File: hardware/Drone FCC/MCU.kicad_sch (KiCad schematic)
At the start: 38 parts, among them SW101 SW RESET, U101 STM32F746ZGTx, Y101 12MHz, Y102 32.768kHz

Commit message: included all components on PCB
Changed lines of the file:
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@@
     (pin "2")
   )
-  (symbol (lib_id "Device:C_Small") (at 173.99 24.765 0) (unit 1)
+  (symbol (lib_id "Device:C_Small") (at 173.99 24.765 0) (mirror y) (unit 1)
     (in_bom yes) (on_board yes) (fields_autoplaced)
     (property "Reference" "C102" (id 0) (at 176.53 23.5012 0)
-      (effects (font (size 1.27 1.27)) (justify left))
+      (effects (font (size 1.27 1.27)) (justify right))
     )
     (property "Value" "100nF" (id 1) (at 176.53 26.0412 0)
-      (effects (font (size 1.27 1.27)) (justify left))
+      (effects (font (size 1.27 1.27)) (justify right))
     )
     (property "Footprint" "Capacitor_SMD:C_0402_1005Metric_Pad0.74x0.62mm_HandSolder" (id 2) (at 173.99 24.765 0)

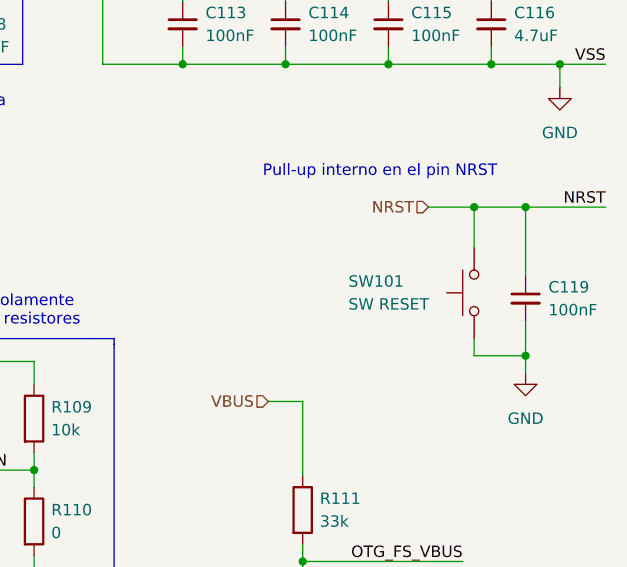
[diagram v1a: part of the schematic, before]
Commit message: add 3D models to footprints
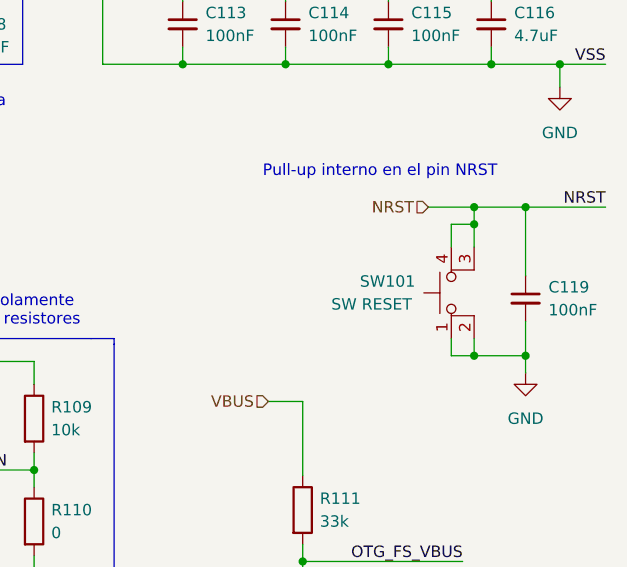
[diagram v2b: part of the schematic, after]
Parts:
- removed SW101: SW RESET, Button_Switch_SMD:SW_SPST_TL3305A, symbol Switch:SW_Push
- added SW101: SW RESET, TL3305AF160QG:SW_TL3305AF160QG, symbol Switch:SW_MEC_5E
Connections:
- net GND: now also SW101.1, SW101.2
- net NRST: now also SW101.3 (K), SW101.4 (A)

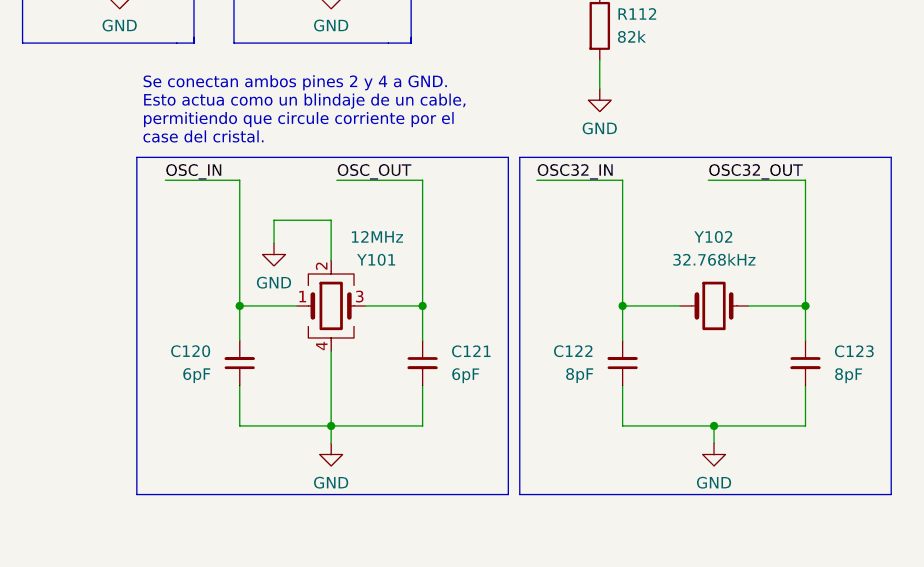
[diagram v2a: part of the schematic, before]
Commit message: routing of HSE crystal oscillator
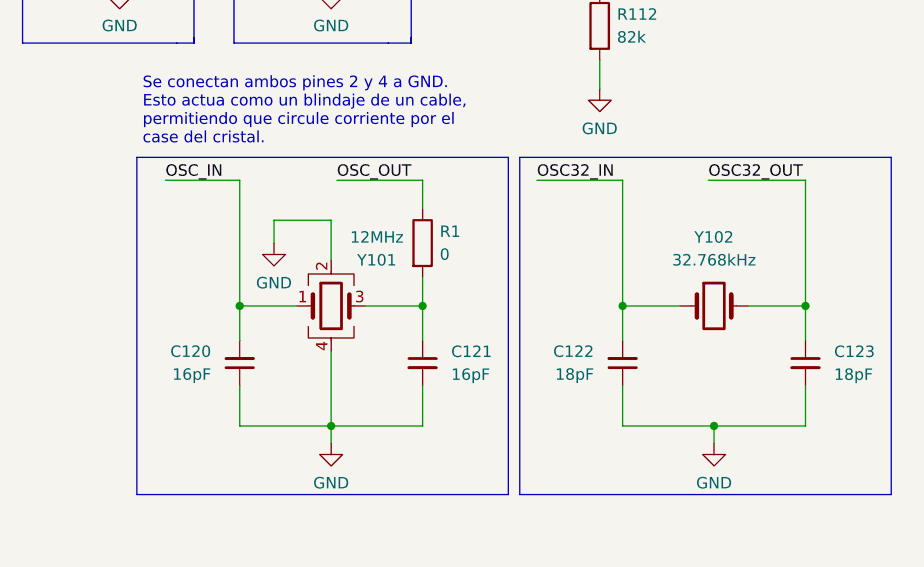
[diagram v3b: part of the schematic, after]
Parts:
- added R1: 0, Resistor_SMD:R_0402_1005Metric_Pad0.72x0.64mm_HandSolder, symbol Device:R
- C120, C121: value 6pF -> 16pF
- C122, C123: value 8pF -> 18pF
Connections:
- net OSC_OUT: now also R1.1; no longer C121.1, Y101.3
- new net: C121.1, R1.2, Y101.3
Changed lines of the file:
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@@
     (stroke (width 0) (type default) (color 0 0 0 0))
   )
-  (wire (pts (xy 229.87 127.635) (xy 229.87 141.605))
+  (wire (pts (xy 229.87 127.635) (xy 229.87 130.81))
     (stroke (width 0) (type default) (color 0 0 0 0))
   )
@@
   )
   (wire (pts (xy 25.4 83.82) (xy 43.18 83.82))
+    (stroke (width 0) (type default) (color 0 0 0 0))
+  )
+  (wire (pts (xy 229.87 138.43) (xy 229.87 141.605))
     (stroke (width 0) (type default) (color 0 0 0 0))
   )
@@
       (effects (font (size 1.27 1.27)) (justify right))
     )
-    (property "Value" "6pF" (id 1) (at 206.375 149.2185 0)
+    (property "Value" "16pF" (id 1) (at 206.375 149.2185 0)
       (effects (font (size 1.27 1.27)) (justify right))
     )
@@
       (effects (font (size 1.27 1.27)) (justify right))
     )
-    (property "Value" "8pF" (id 1) (at 248.92 149.2185 0)
+    (property "Value" "18pF" (id 1) (at 248.92 149.2185 0)
       (effects (font (size 1.27 1.27)) (justify right))
     )
@@
     )
     (property "Datasheet" "~" (id 3) (at 259.08 22.225 0)
+      (effects (font (size 1.27 1.27)) hide)
+    )
+    (pin "1")
+    (pin "2")
+  )
+  (symbol (lib_id "Device:R") (at 229.87 134.62 0) (unit 1)
+    (in_bom yes) (on_board yes) (fields_autoplaced)
+    (property "Reference" "R1" (id 0) (at 231.775 133.3499 0)
+      (effects (font (size 1.27 1.27)) (justify left))
+    )
+    (property "Value" "0" (id 1) (at 231.775 135.8899 0)
+      (effects (font (size 1.27 1.27)) (justify left))
+    )
+    (property "Footprint" "Resistor_SMD:R_0402_1005Metric_Pad0.72x0.64mm_HandSolder" (id 2) (at 228.092 134.62 90)
+      (effects (font (size 1.27 1.27)) hide)
+    )
+    (property "Datasheet" "~" (id 3) (at 229.87 134.62 0)
       (effects (font (size 1.27 1.27)) hide)
     )
@@
       (effects (font (size 1.27 1.27)) (justify left))
     )
-    (property "Value" "6pF" (id 1) (at 233.045 149.2312 0)
+    (property "Value" "16pF" (id 1) (at 233.045 149.2312 0)
       (effects (font (size 1.27 1.27)) (justify left))
     )
@@
       (effects (font (size 1.27 1.27)) (justify left))
     )
-    (property "Value" "8pF" (id 1) (at 275.59 149.2312 0)
-      (effects (font (size 1.27 1.27)) (justify left))
-    )
+    (property "Value" "18pF" (id 1) (at 275.59 149.2312 0)
+      (effects (font (size 1.27 1.27)) (justify left))
+    )

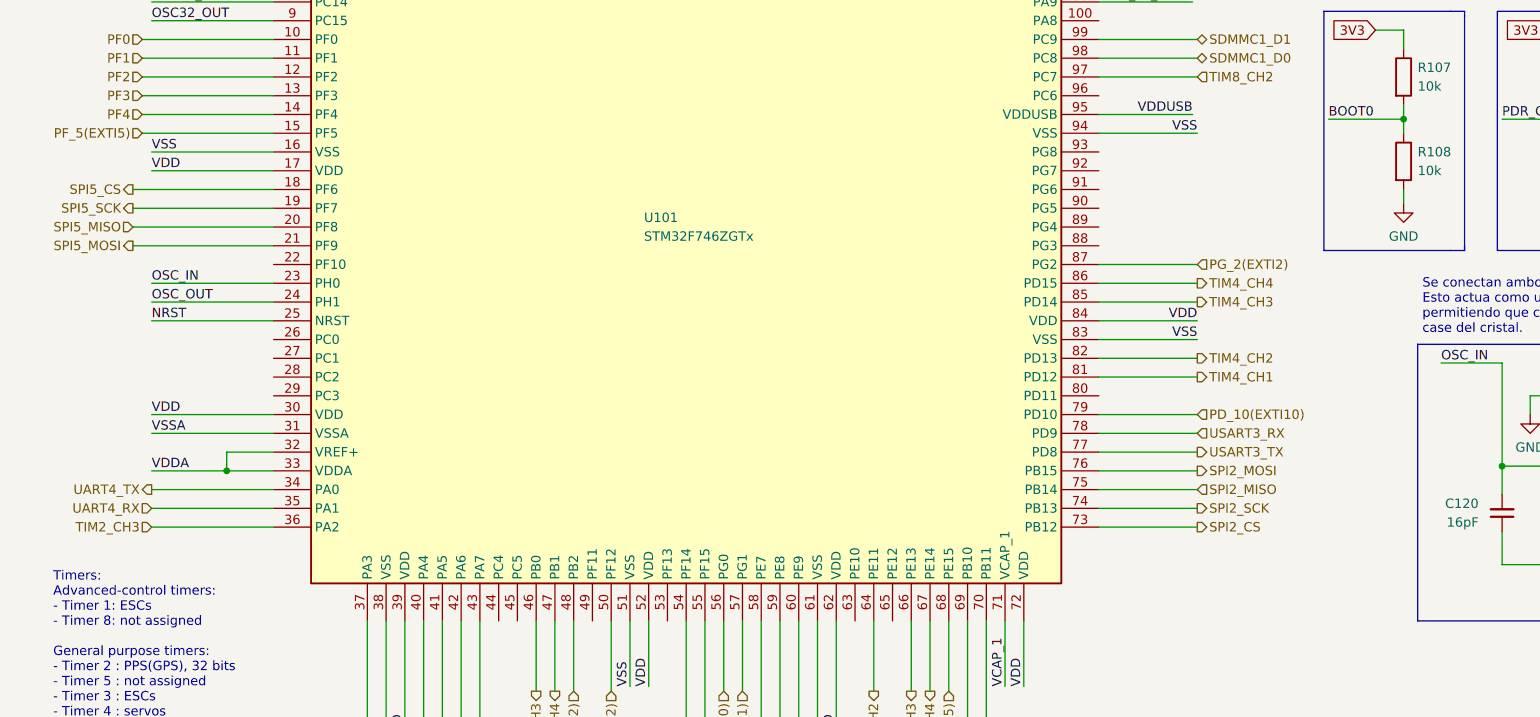
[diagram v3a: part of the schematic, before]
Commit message: add series resistor SPI buses
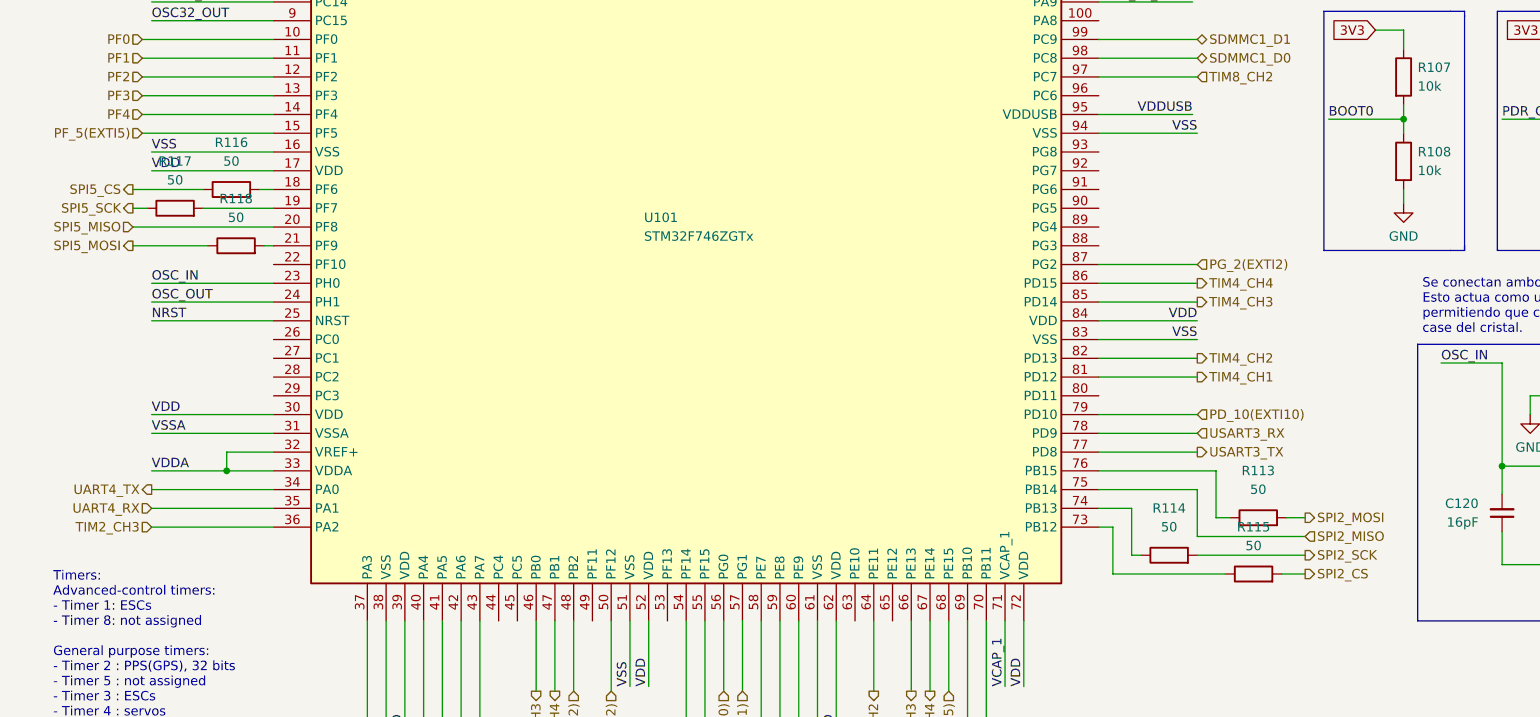
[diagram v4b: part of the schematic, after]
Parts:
- added R113, R114, R115, R116, R117, R118: 50, Resistor_SMD:R_0402_1005Metric_Pad0.72x0.64mm_HandSolder, symbol Device:R
- C119: footprint Capacitor_SMD:C_0603_1608Metric_Pad1.08x0.95mm_HandSolder -> Capacitor_SMD:C_0402_1005Metric_Pad0.74x0.62mm_HandSolder
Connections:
- net SPI2_CS: now also R115.2; no longer U101.73 (PB12)
- net SPI2_MOSI: now also R113.2; no longer U101.76 (PB15)
- net SPI2_SCK: now also R114.2; no longer U101.74 (PB13)
- net SPI5_CS: now also R116.1; no longer U101.18 (PF6)
- net SPI5_MOSI: now also R118.1; no longer U101.21 (PF9)
- net SPI5_SCK: now also R117.1; no longer U101.19 (PF7)
- new net: R117.2, U101.19 (PF7)
- new net: R114.1, U101.74 (PB13)
- new net: R116.2, U101.18 (PF6)
- new net: R118.2, U101.21 (PF9)
- new net: R115.1, U101.73 (PB12)
- new net: R113.1, U101.76 (PB15)

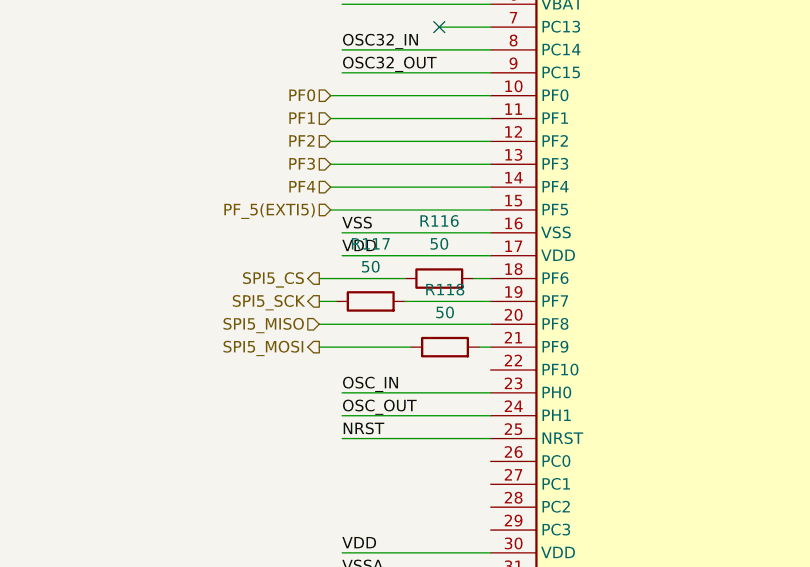
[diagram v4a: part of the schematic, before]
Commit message: add TVS diodes for SPI and ESD capacitors
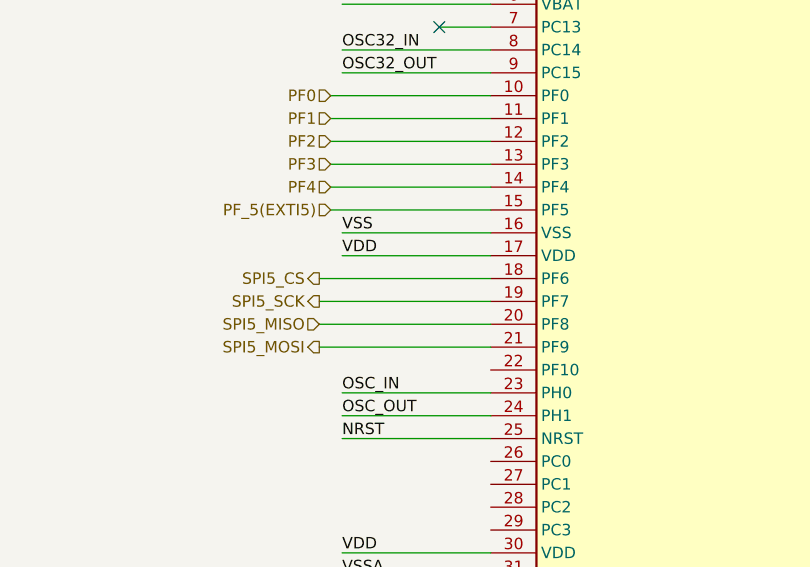
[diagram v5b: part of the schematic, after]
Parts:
- removed R116, R117, R118: 50, Resistor_SMD:R_0402_1005Metric_Pad0.72x0.64mm_HandSolder, symbol Device:R
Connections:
- net SPI5_CS: now also U101.18 (PF6)
- net SPI5_MOSI: now also U101.21 (PF9)
- net SPI5_SCK: now also U101.19 (PF7)
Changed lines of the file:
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@@
-    (stroke (width 0) (type default) (color 0 0 0 0))
-  )
-  (wire (pts (xy 24.13 111.76) (xy 34.29 111.76))
     (stroke (width 0) (type default) (color 0 0 0 0))
   )
@@
     (stroke (width 0) (type default) (color 0 0 0 0))
   )
-  (wire (pts (xy 33.655 106.68) (xy 43.18 106.68))
-    (stroke (width 0) (type default) (color 0 0 0 0))
-  )
   (wire (pts (xy 259.08 49.53) (xy 270.51 49.53))
     (stroke (width 0) (type default) (color 0 0 0 0))
@@
     (stroke (width 0) (type default) (color 0 0 0 0))
   )
-  (wire (pts (xy 41.91 111.76) (xy 43.18 111.76))
+  (wire (pts (xy 24.13 111.76) (xy 43.18 111.76))
     (stroke (width 0) (type default) (color 0 0 0 0))
   )
@@
     (stroke (width 0) (type default) (color 0 0 0 0))
   )
-  (wire (pts (xy 24.13 106.68) (xy 26.035 106.68))
+  (wire (pts (xy 24.13 106.68) (xy 43.18 106.68))
     (stroke (width 0) (type default) (color 0 0 0 0))
   )
@@
     (stroke (width 0) (type default) (color 0 0 0 0))
   )
-  (wire (pts (xy 41.275 104.14) (xy 43.18 104.14))
-    (stroke (width 0) (type default) (color 0 0 0 0))
-  )
   (polyline (pts (xy 208.915 80.01) (xy 226.06 80.01))
     (stroke (width 0) (type default) (color 0 0 0 0))
@@
     (stroke (width 0) (type default) (color 0 0 0 0))
   )
-  (wire (pts (xy 24.13 104.14) (xy 33.655 104.14))
+  (wire (pts (xy 24.13 104.14) (xy 43.18 104.14))
     (stroke (width 0) (type default) (color 0 0 0 0))
   )
@@
     )
     (property "Datasheet" "~" (id 3) (at 229.87 134.62 0)
-      (effects (font (size 1.27 1.27)) hide)
-    )
-    (pin "1")
-    (pin "2")
-  )
-  (symbol (lib_id "Device:R") (at 29.845 106.68 90) (unit 1)
-    (in_bom yes) (on_board yes) (fields_autoplaced)
-    (property "Reference" "R117" (id 0) (at 29.845 100.33 90))
-    (property "Value" "50" (id 1) (at 29.845 102.87 90))
-    (property "Footprint" "Resistor_SMD:R_0402_1005Metric_Pad0.72x0.64mm_HandSolder" (id 2) (at 29.845 108.458 90)
-      (effects (font (size 1.27 1.27)) hide)
-    )
-    (property "Datasheet" "~" (id 3) (at 29.845 106.68 0)
       (effects (font (size 1.27 1.27)) hide)
     )
@@
     (pin "99")
   )
-  (symbol (lib_id "Device:R") (at 37.465 104.14 90) (unit 1)
-    (in_bom yes) (on_board yes) (fields_autoplaced)
-    (property "Reference" "R116" (id 0) (at 37.465 97.79 90))
-    (property "Value" "50" (id 1) (at 37.465 100.33 90))
-    (property "Footprint" "Resistor_SMD:R_0402_1005Metric_Pad0.72x0.64mm_HandSolder" (id 2) (at 37.465 105.918 90)
-      (effects (font (size 1.27 1.27)) hide)
-    )
-    (property "Datasheet" "~" (id 3) (at 37.465 104.14 0)
-      (effects (font (size 1.27 1.27)) hide)
-    )
-    (pin "1")
-    (pin "2")
-  )
   (symbol (lib_id "Device:C_Small") (at 236.22 22.225 0) (unit 1)
     (in_bom yes) (on_board yes) (fields_autoplaced)
@@
       (effects (font (size 1.27 1.27)) hide)
     )
-    (pin "1")
-    (pin "2")
-  )
-  (symbol (lib_id "Device:R") (at 38.1 111.76 90) (unit 1)
-    (in_bom yes) (on_board yes) (fields_autoplaced)
-    (property "Reference" "R118" (id 0) (at 38.1 105.41 90))
-    (property "Value" "50" (id 1) (at 38.1 107.95 90))
-    (property "Footprint" "Resistor_SMD:R_0402_1005Metric_Pad0.72x0.64mm_HandSolder" (id 2) (at 38.1 113.538 90)
-      (effects (font (size 1.27 1.27)) hide)
-    )
-    (property "Datasheet" "~" (id 3) (at 38.1 111.76 0)
-      (effects (font (size 1.27 1.27)) hide)
-    )

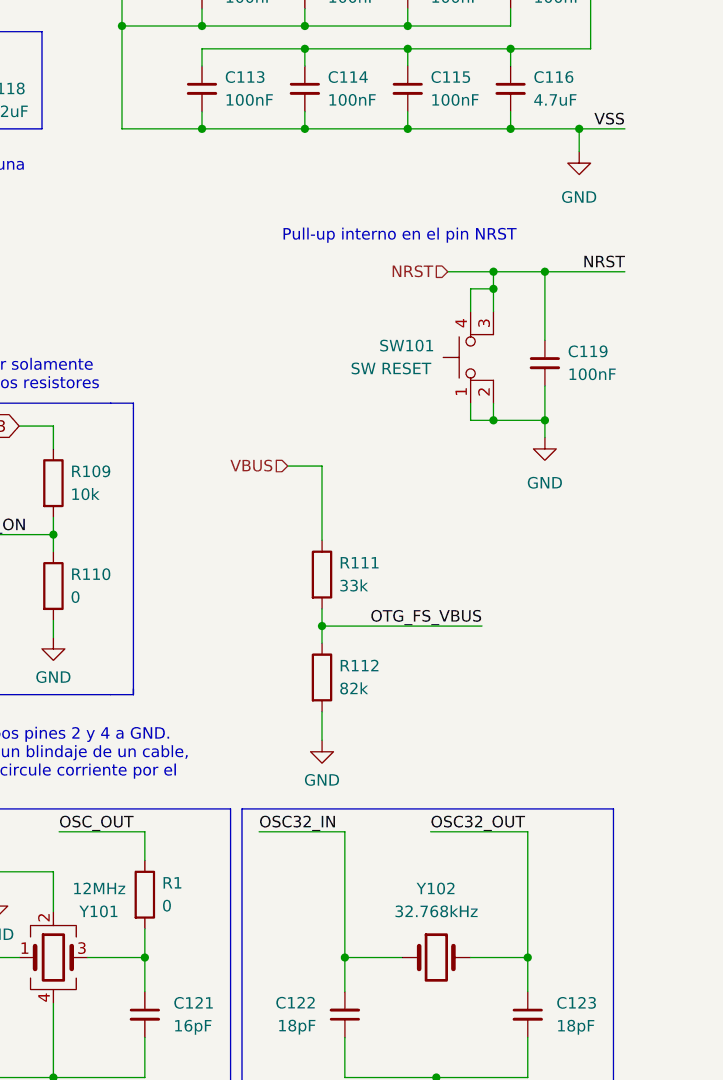
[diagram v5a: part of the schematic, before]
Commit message: added missing TVS diodes
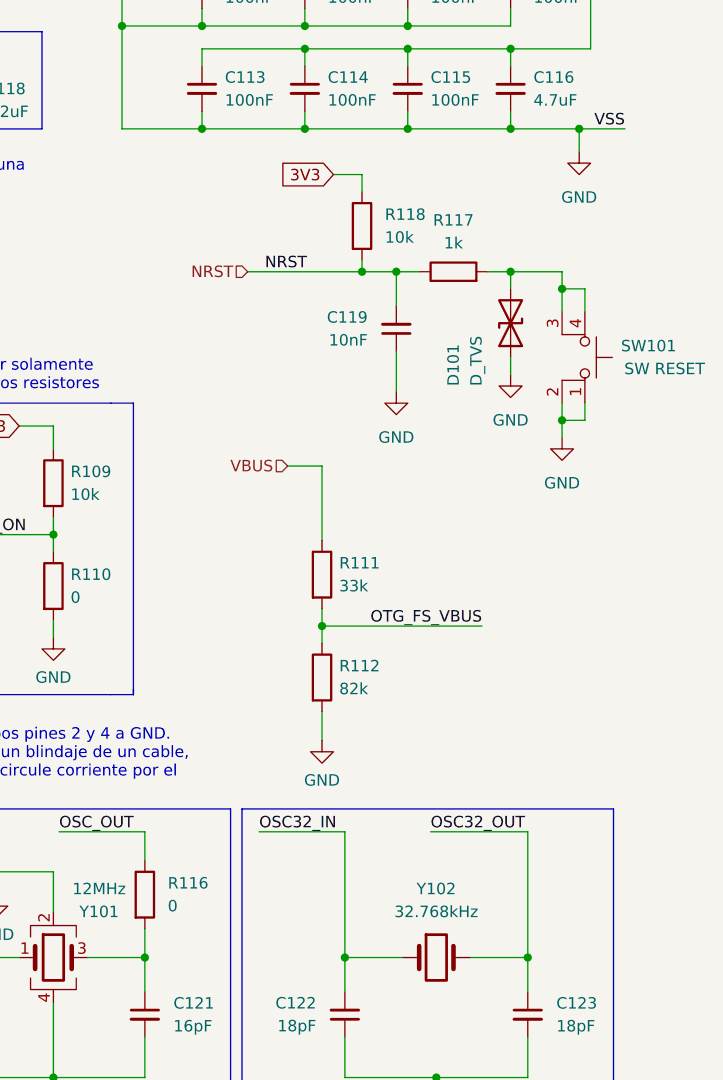
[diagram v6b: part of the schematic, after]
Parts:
- added D101: D_TVS, Diode_SMD:D_0402_1005Metric_Pad0.77x0.64mm_HandSolder, symbol Device:D_TVS
- added R117: 1k, Resistor_SMD:R_0402_1005Metric_Pad0.72x0.64mm_HandSolder, symbol Device:R
- added R118: 10k, Resistor_SMD:R_0402_1005Metric_Pad0.72x0.64mm_HandSolder, symbol Device:R
- C117, C118: footprint Capacitor_SMD:C_0603_1608Metric_Pad1.08x0.95mm_HandSolder -> Capacitor_SMD:C_0402_1005Metric_Pad0.74x0.62mm_HandSolder
- C119: value 100nF -> 10nF
- renumbered R1 to R116
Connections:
- net 3V3: now also R118.1
- net GND: now also C119.1, D101.1 (A1); no longer C119.2
- net NRST: now also C119.2, R117.1, R118.2; no longer C119.1, SW101.3 (K), SW101.4 (A)
- new net: D101.2 (A2), R117.2, SW101.3 (K), SW101.4 (A)
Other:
- note removed: "Pull-up interno en el pin NRST"
- moved on the sheet: C119, SW101
